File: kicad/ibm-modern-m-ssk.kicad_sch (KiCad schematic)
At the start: 0 parts

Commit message: Add matrix schematic and update project structure
Added new matrix.kicad_sch schematic file and integrated it as a subsheet in ibm-modern-m-ssk.kicad_sch. Updated project and schematic settings in ibm-modern-m-ssk.kicad_pro and adjusted selection filters in ibm-modern-m-ssk.kicad_prl to reflect the new structure.
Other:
- added sheet matrix (matrix.kicad_sch)
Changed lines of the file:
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@@
 	(generator_version "9.0")
 	(paper "A4")
+	(sheet
+		(at 241.3 38.1)
+		(size 12.7 12.7)
+		(exclude_from_sim no)
+		(in_bom yes)
+		(on_board yes)
+		(dnp no)
+		(fields_autoplaced yes)
+		(stroke
+			(width 0.1524)
+			(type solid)
+		)
+		(fill
+			(color 0 0 0 0.0000)
+		)
+		(property "Sheetname" "matrix"
+			(at 241.3 37.3884 0)
+			(effects
+				(font
+					(size 1.27 1.27)
+				)
+				(justify left bottom)
+			)
+		)
+		(property "Sheetfile" "matrix.kicad_sch"
+			(at 241.3 51.3846 0)
+			(effects
+				(font
+					(size 1.27 1.27)
+				)
+				(justify left top)
+			)
+		)
+		(instances
+			(project "ibm-modern-m-ssk"
+				(path "/17f6a4a5-fbff-4e30-a1cc-9481373e4968"
+					(page "2")
+				)
+			)
+		)
+	)
 	(sheet_instances
 		(path "/"

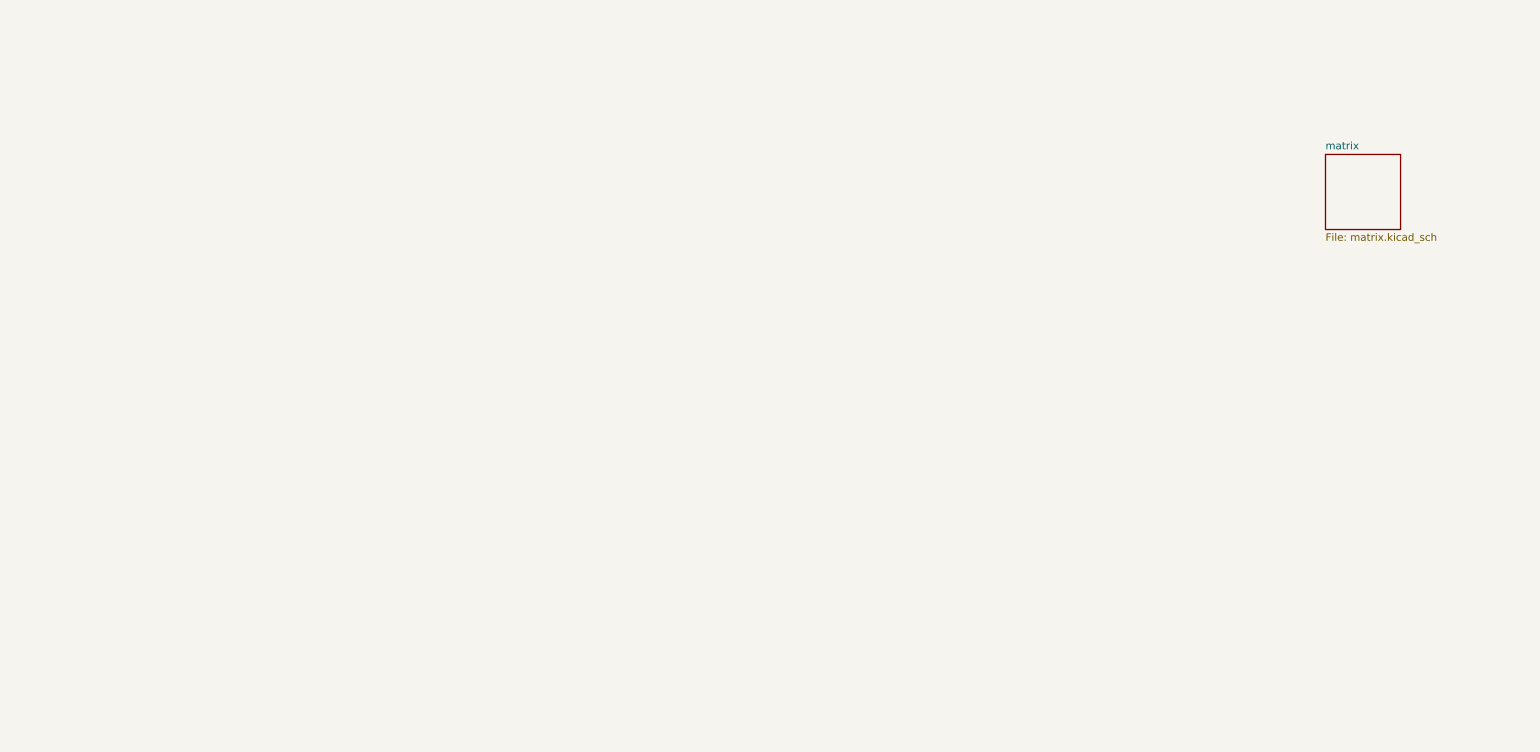
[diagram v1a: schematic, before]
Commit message: Add new symbols to schematic and update selection filter
Added symbols for MCP73831-2-OT, USB_C_Receptacle_USB2.0_14P, R_Small, and MDBT50Q-1MV2 to ibm-modern-m-ssk.kicad_sch. Updated selection filter in ibm-modern-m-ssk.kicad_prl to enable all item types. Removed an old backup zip and renamed a lock file.
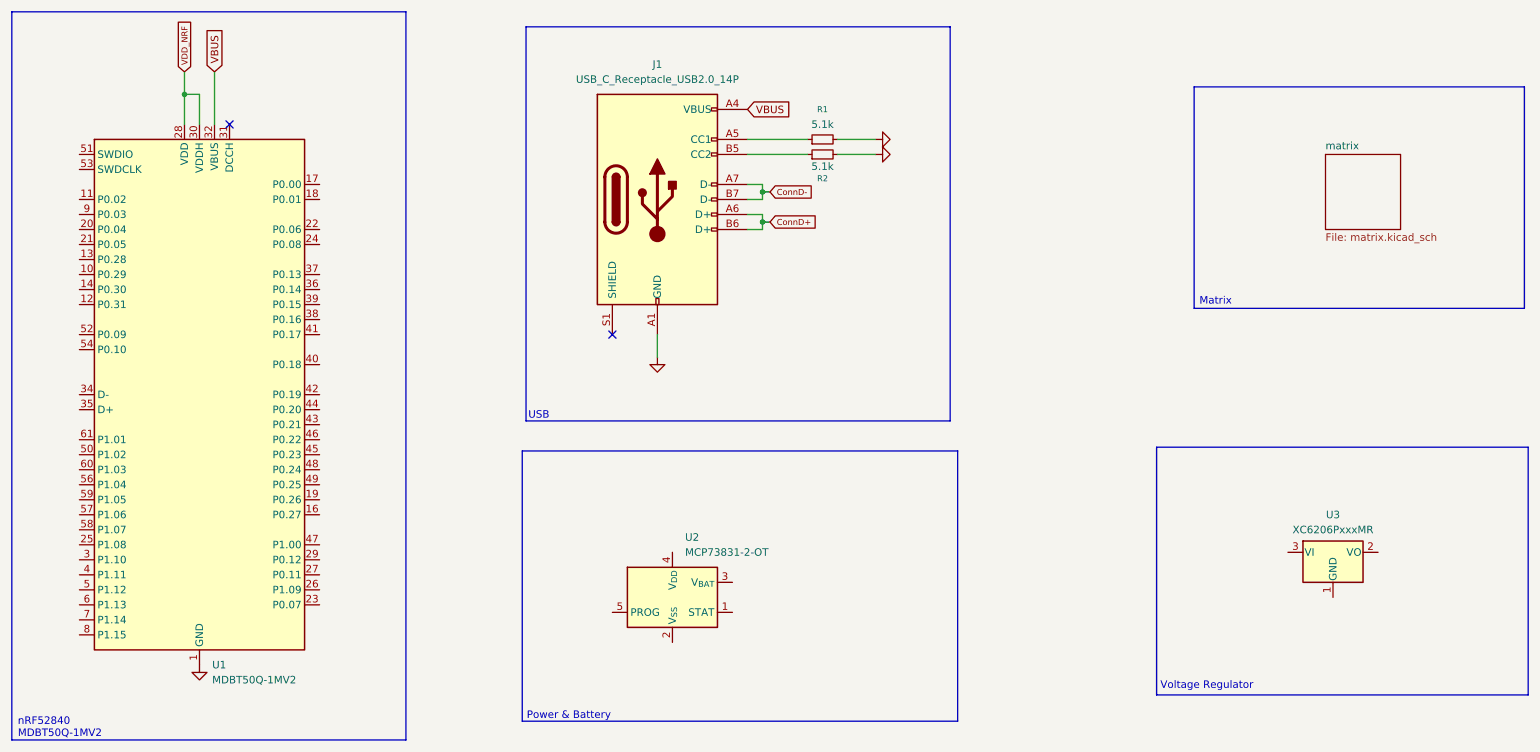
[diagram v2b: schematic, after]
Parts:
- added J1: USB_C_Receptacle_USB2.0_14P, PCM_marbastlib-various:USB_C_Receptacle_HRO_TYPE-C-31-M-12, symbol Connector:USB_C_Receptacle_USB2.0_14P
- added R1, R2: 5.1k, symbol Device:R_Small
- added U1: MDBT50Q-1MV2, RF_Module:Raytac_MDBT50Q, symbol RF_Module:MDBT50Q-1MV2
- added U2: MCP73831-2-OT, Package_TO_SOT_SMD:SOT-23-5, symbol Battery_Management:MCP73831-2-OT
- added U3: XC6206PxxxMR, Package_TO_SOT_SMD:SOT-23-3, symbol Regulator_Linear:XC6206PxxxMR
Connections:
- new net: J1.A5 (CC1), R1.1
- new net: J1.B5 (CC2), R2.1
- new net ConnD+: J1.A6 (D+), J1.B6 (D+)
- new net ConnD-: J1.A7 (D-), J1.B7 (D-)
- new net GND: J1.A1 (GND), J1.A12 (GND), J1.B1 (GND), J1.B12 (GND), R1.2, R2.2, U1.1 (GND), U1.15 (GND), U1.2 (GND), U1.33 (GND), U1.55 (GND)
- new net VBUS: J1.A4 (VBUS), J1.A9 (VBUS), J1.B4 (VBUS), J1.B9 (VBUS), U1.32 (VBUS)
- new net VDD_NRF: U1.28 (VDD), U1.30 (VDDH)
- no-connect marks 0 -> 2
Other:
- note added: "Matrix"
- note added: "Power & Battery"
- note added: "USB"
- note added: "Voltage Regulator"
- note added: "nRF52840 MDBT50Q-1MV2"

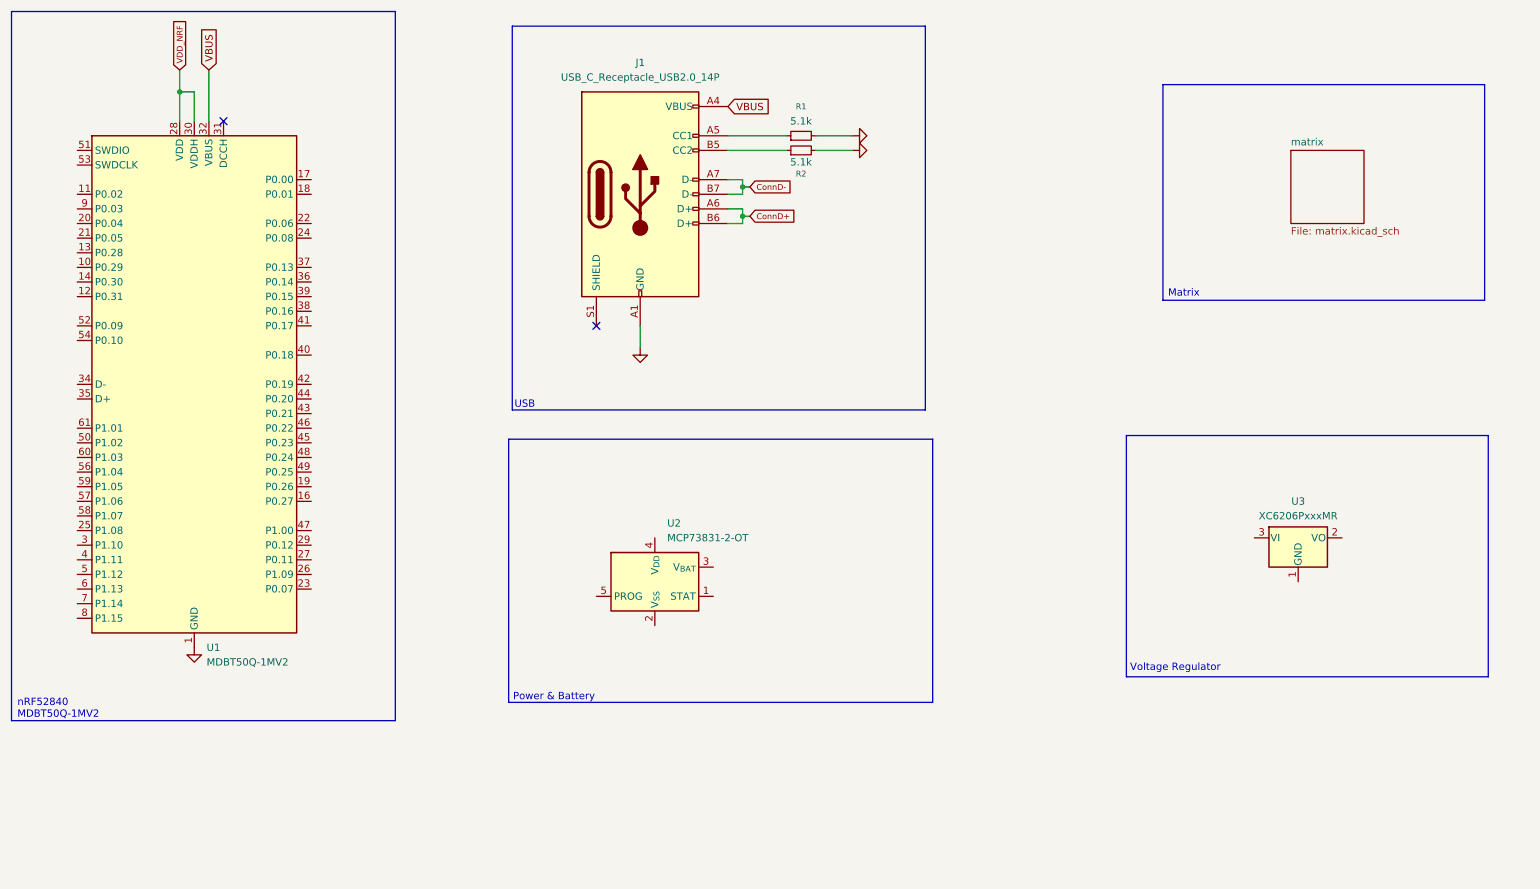
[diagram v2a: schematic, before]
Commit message: Add new connectors and components to schematic
Added symbols for Conn_01x02_Socket, Conn_02x06_Odd_Even, C_Small, Crystal_Small, LED_Small_Filled, and USBLC6-2P6 to ibm-modern-m-ssk.kicad_sch. Updated schematic to include these components. Added backup, autosave, and lock files, as well as new measurement scans in the measurments directory.
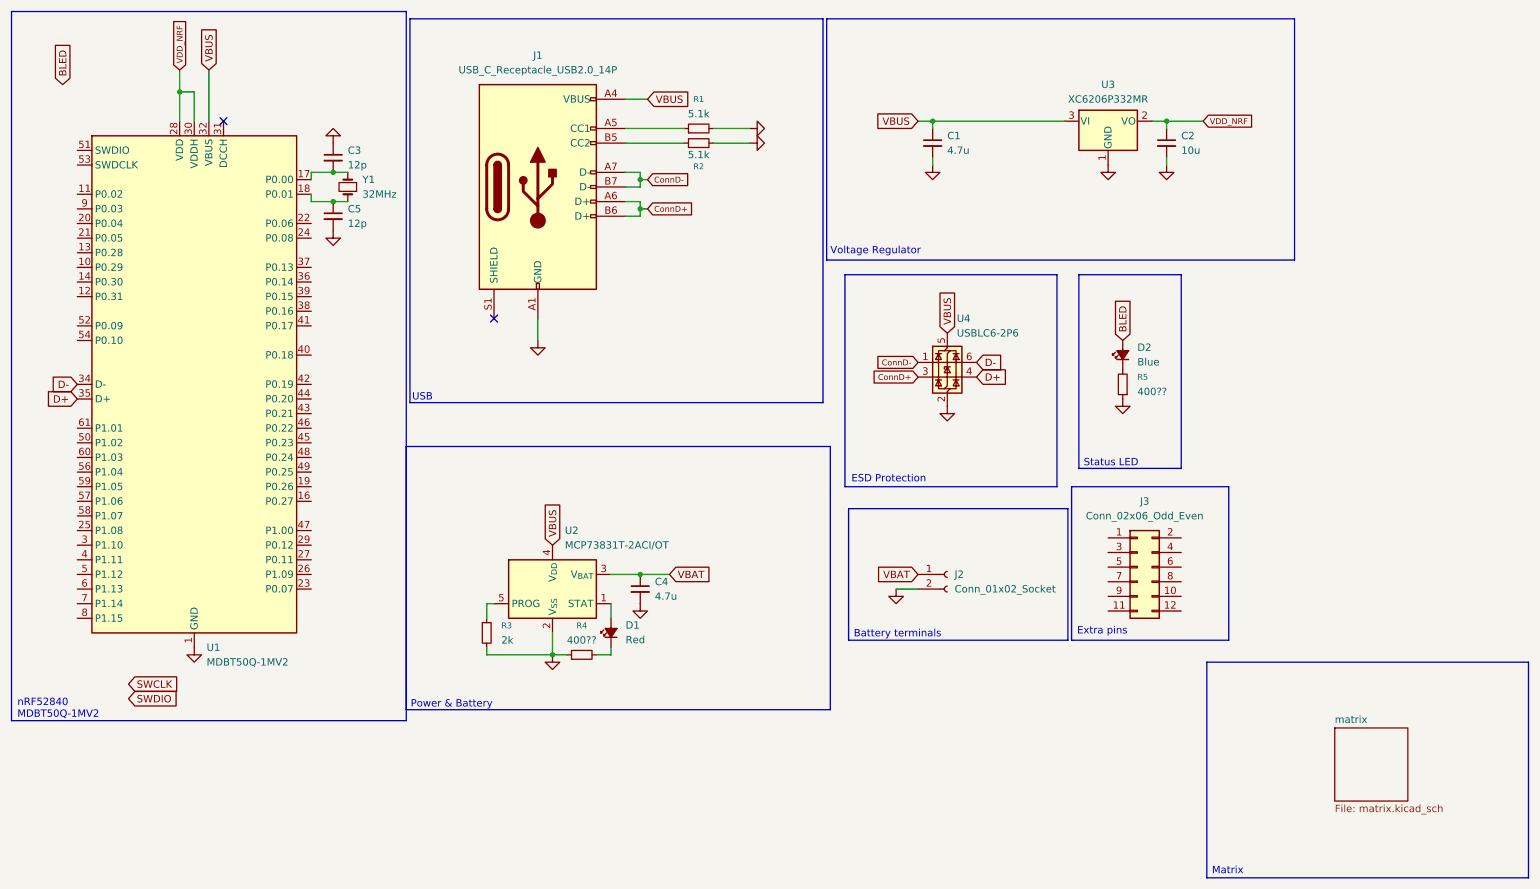
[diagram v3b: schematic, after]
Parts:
- added C1, C4: 4.7u, symbol Device:C_Small
- added C2: 10u, symbol Device:C_Small
- added C3, C5: 12p, symbol Device:C_Small
- added D1: Red, symbol Device:LED_Small_Filled
- added D2: Blue, symbol Device:LED_Small_Filled
- added J2: Conn_01x02_Socket, symbol Connector:Conn_01x02_Socket
- added J3: Conn_02x06_Odd_Even, symbol Connector_Generic:Conn_02x06_Odd_Even
- added R3: 2k, symbol Device:R_Small
- added R4, R5: 400??, symbol Device:R_Small
- added U4: USBLC6-2P6, Package_TO_SOT_SMD:SOT-666, symbol Power_Protection:USBLC6-2P6
- added Y1: 32MHz, symbol Device:Crystal_Small
- U2: value MCP73831-2-OT -> MCP73831T-2ACI/OT
- U3: value XC6206PxxxMR -> XC6206P332MR
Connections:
- net ConnD+: now also U4.3 (I/O2)
- net ConnD-: now also U4.1 (I/O1)
- net GND: now also U2.2 (V_{SS}), U3.1 (GND), C1.2, C2.2, C3.1, C4.2, C5.2, J2.2 (Pin_2), R3.2, R4.1, R5.1, U4.2 (GND)
- net VBUS: now also U2.4 (V_{DD}), U3.3 (VI), C1.1, U4.5 (VBUS)
- net VDD_NRF: now also U3.2 (VO), C2.1
- net at U2.1 (STAT): now also D1.2 (A)
- net VBAT: now reaches U2.3 (V_{BAT})
- net VBAT: now also C4.1, J2.1 (Pin_1)
- net at U2.5 (PROG): now also R3.1
- net at U1.17 (P0.00): now also C3.2, Y1.2
- net at U1.18 (P0.01): now also C5.1, Y1.1
- net D-: now reaches U1.34 (D-)
- net D-: now also U4.6 (I/O1)
- net D+: now reaches U1.35 (D+)
- net D+: now also U4.4 (I/O2)
- new net: D1.1 (K), R4.2
- new net: D2.1 (K), R5.2
- new net BLED: D2.2 (A)
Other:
- note added: "Battery terminals"
- note added: "ESD Protection"
- note added: "Extra pins"
- note added: "Status LED"
- moved on the sheet: J1, R1, R2, U2, U3
